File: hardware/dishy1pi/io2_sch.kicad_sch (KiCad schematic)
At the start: 31 parts, among them CN6 KF2EDGR-2.54-9P, CN7 KF2EDGR-2.54-6P, U10 LTV-827S-TA1, U11 LTV-817S-TA1, U12 LTV-817S-TA1, U9 LTV-847S

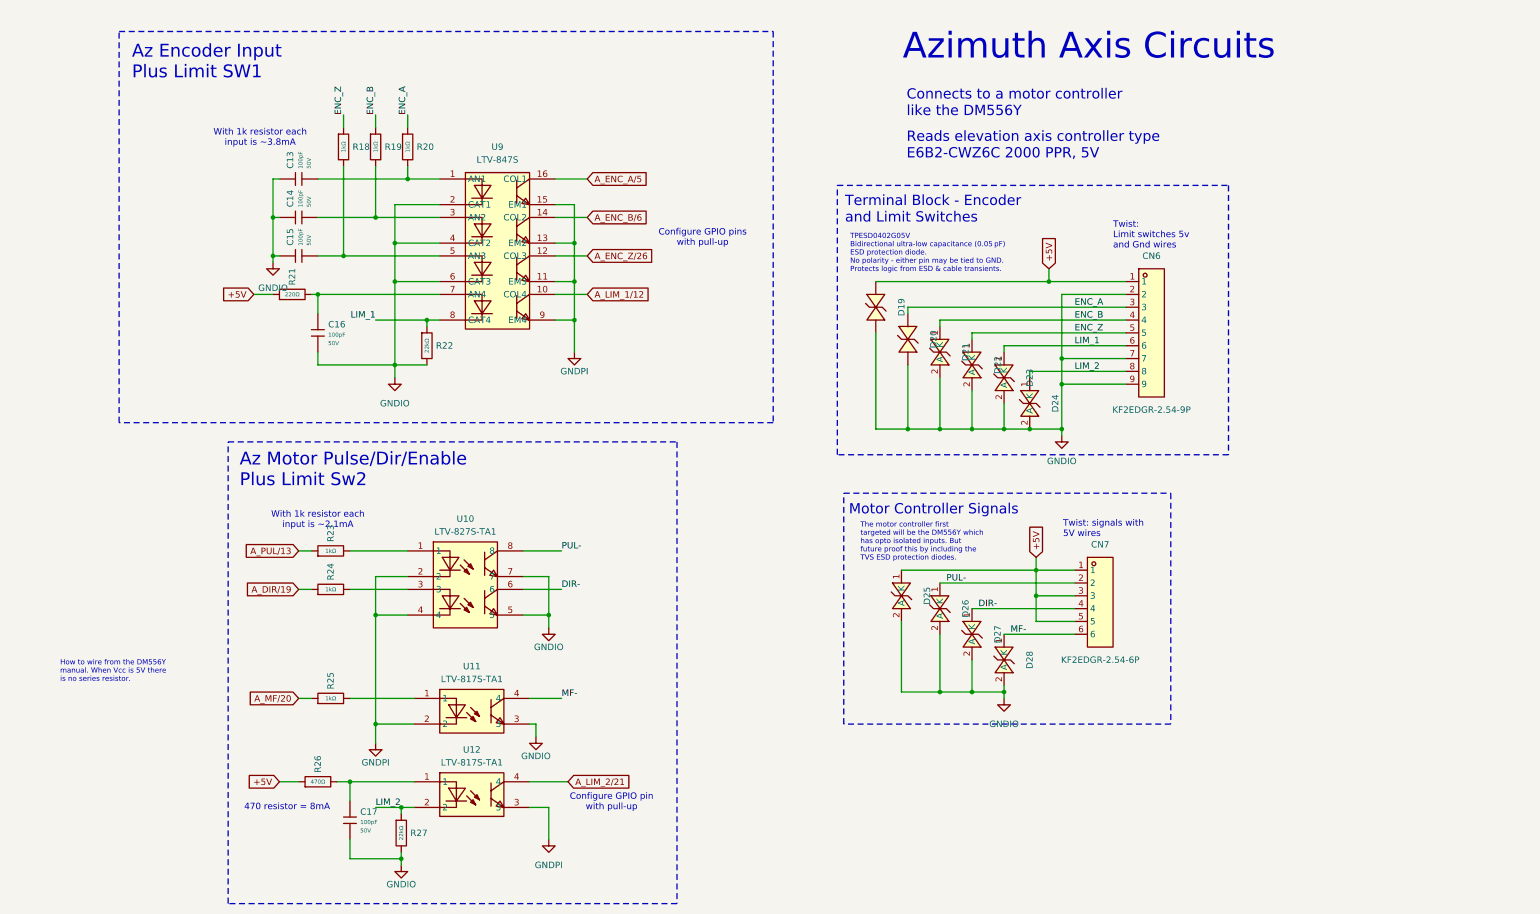
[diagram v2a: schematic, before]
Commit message: Modifications based on first board assembly
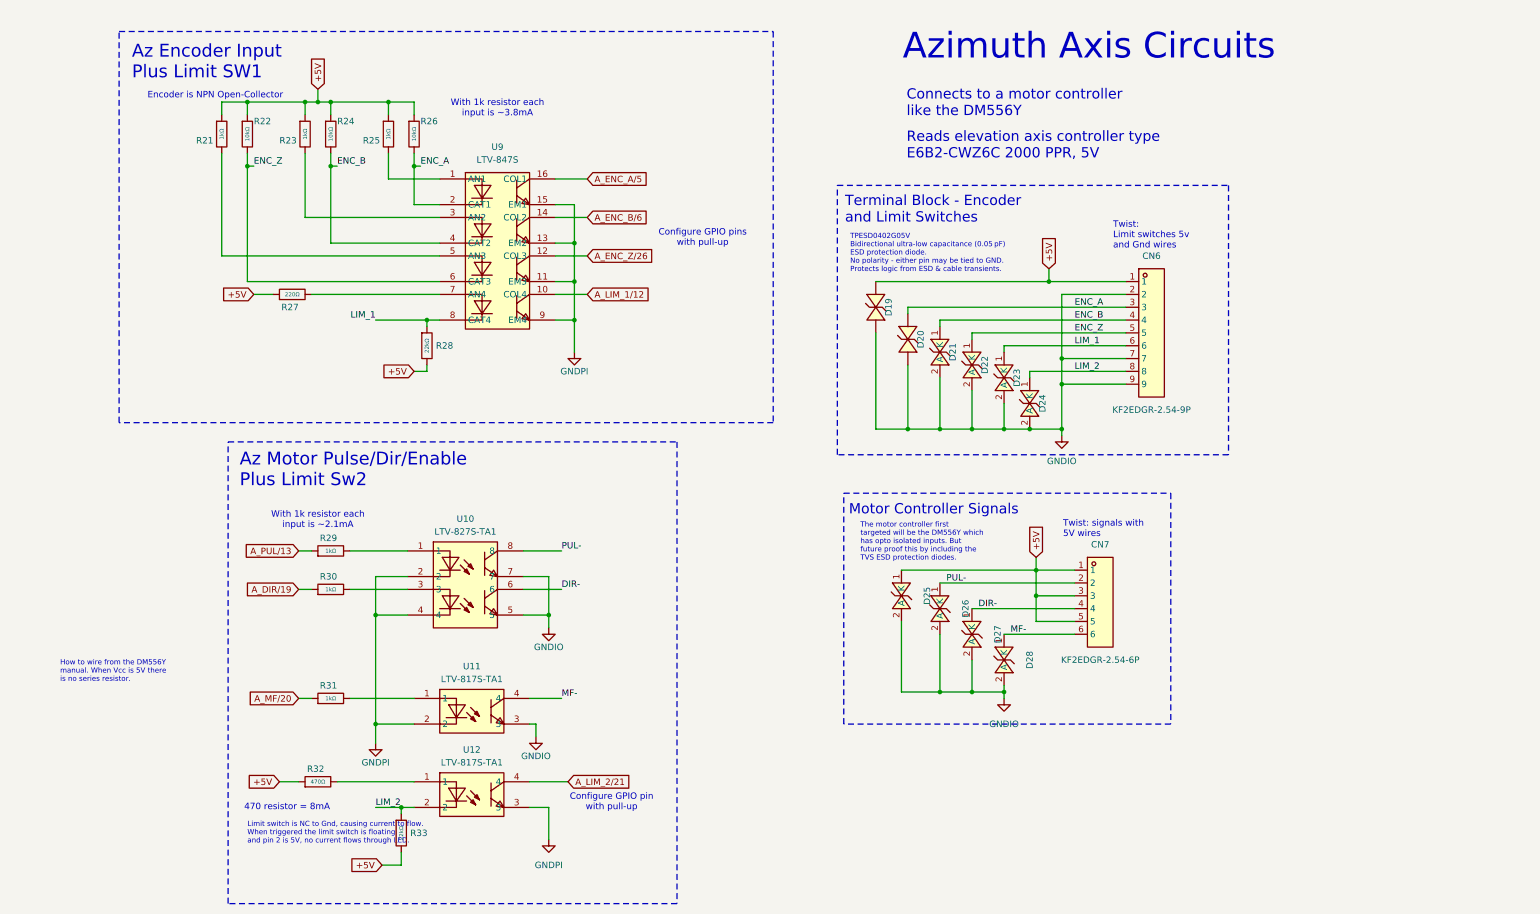
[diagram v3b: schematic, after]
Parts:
- removed C13, C14, C15, C16, C17: 100pF, PCM_JLCPCB:C_0402, symbol PCM_JLCPCB-Capacitors:0402,100pF
- removed R18, R19, R20: 1kΩ, PCM_JLCPCB:R_0402, symbol PCM_JLCPCB-Resistors:0402,1kΩ
- added R21, R23, R25: 1kΩ, PCM_JLCPCB:R_0402, symbol PCM_JLCPCB-Resistors:0402,1kΩ
- added R22, R24, R26: 10kΩ, PCM_JLCPCB:R_0402, symbol PCM_JLCPCB-Resistors:0402,10kΩ
- renumbered R21 to R27, R22 to R28, R23 to R29, R24 to R30, R25 to R31, R26 to R32, R27 to R33
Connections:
- net +5V: now also R28.2, R33.2, R21.1, R22.1, R23.1, R24.1, R25.1, R26.1
- net ENC_A: now also U9.2 (CAT1), R26.2
- net ENC_B: now also U9.4 (CAT2), R24.2
- net ENC_Z: now also U9.6 (CAT3), R22.2
- net GNDIO: no longer R28.2, R33.2, U9.2 (CAT1), U9.4 (CAT2), U9.6 (CAT3)
- net at U9.1 (AN1): now also R25.2
- net at U9.3 (AN2): now also R23.2
- net at U9.5 (AN3): now also R21.2
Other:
- note added: "Encoder is NPN Open-Collector"
- note added: "Limit switch is NC to Gnd, causing current to flow. When triggered the limit switch is floating and pin 2 is 5V, no current flows through LED."

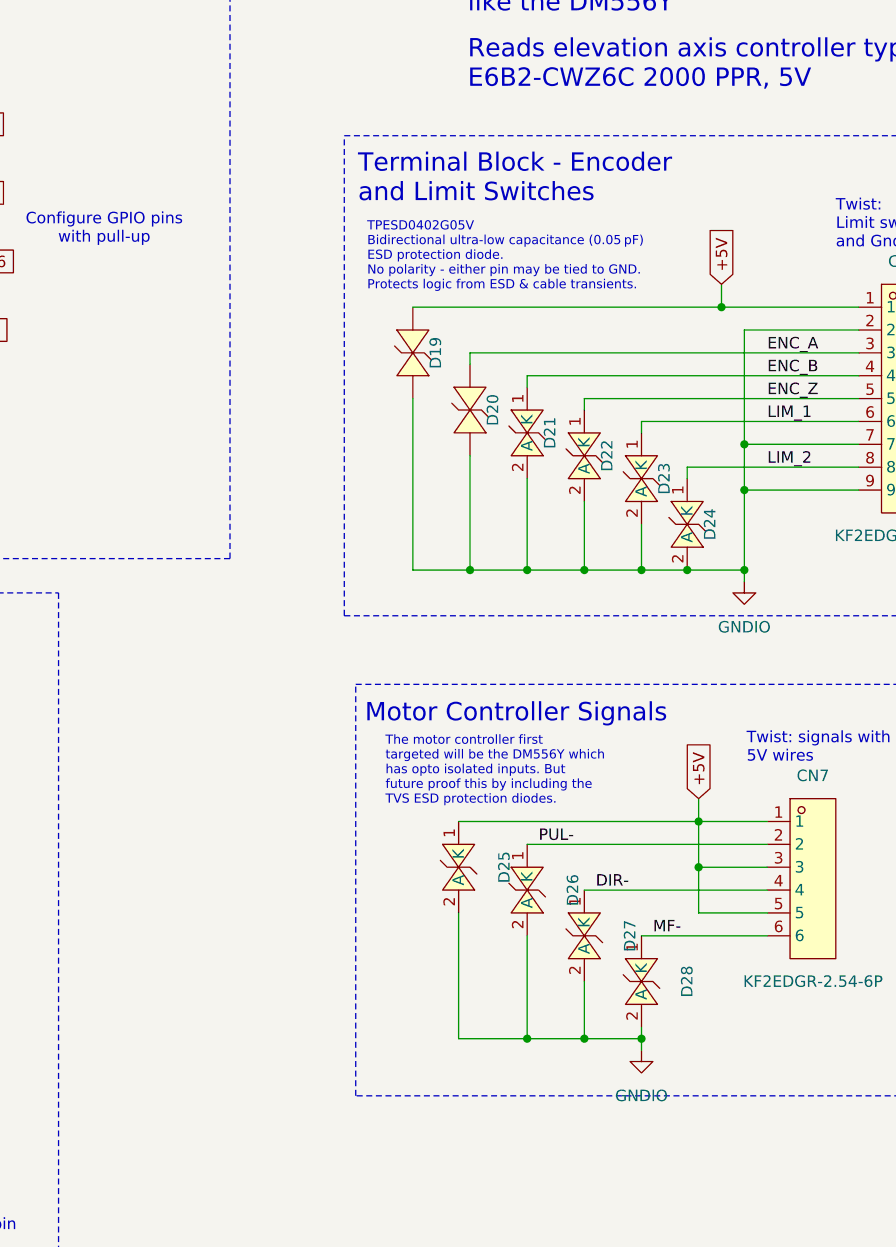
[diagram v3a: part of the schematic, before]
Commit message: Added power circuit to dishy schematic
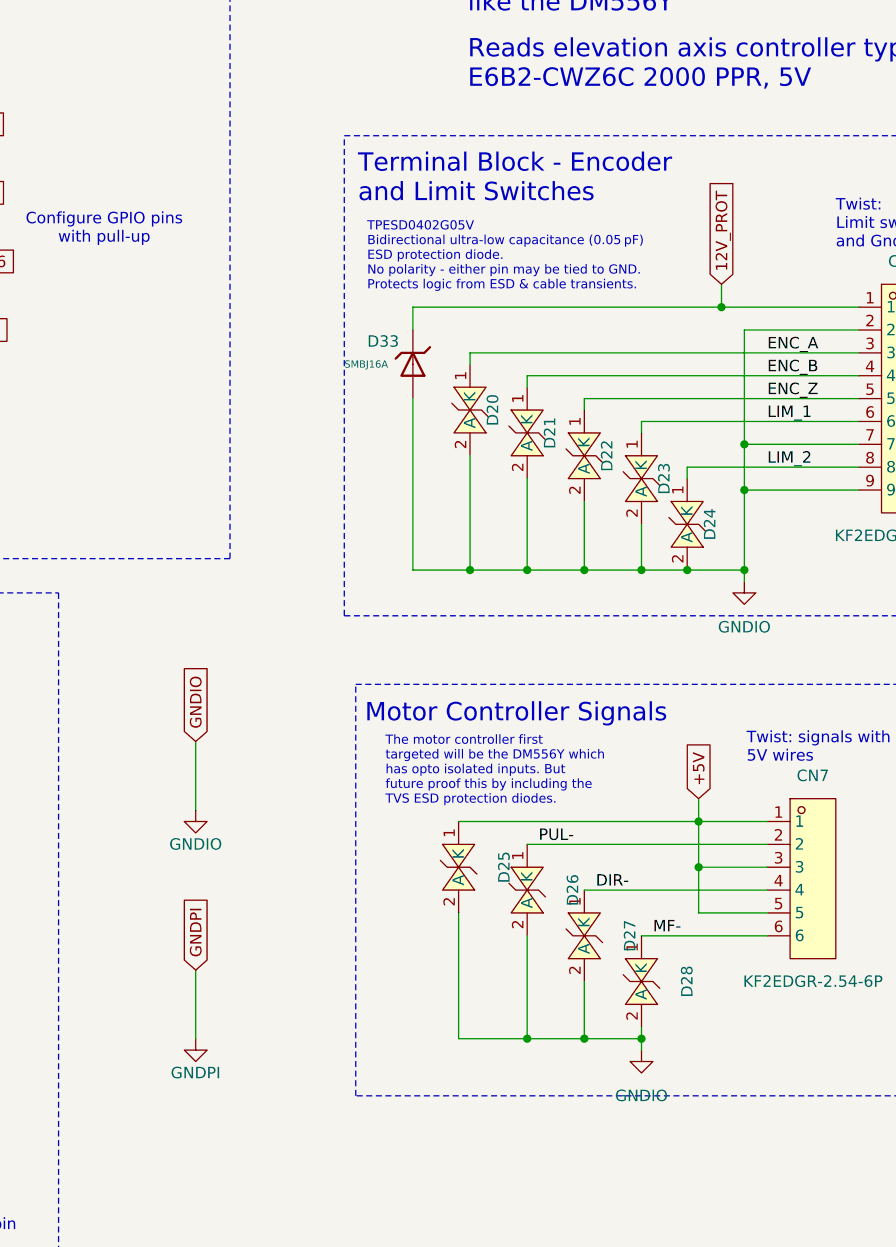
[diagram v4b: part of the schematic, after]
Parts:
- removed D19: TPESD0402G05V, MyParts:D0402-BI, symbol MyParts:TPESD0402G05V
- added D33: SMBJ16A, PCM_JLCPCB:D_SMB, symbol PCM_JLCPCB-Diodes:TVS-Uni,SMBJ16A
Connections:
- net +5V: no longer CN6.1
- net GNDIO: now also D33.2
- new net 12V_PROT: CN6.1, D33.1

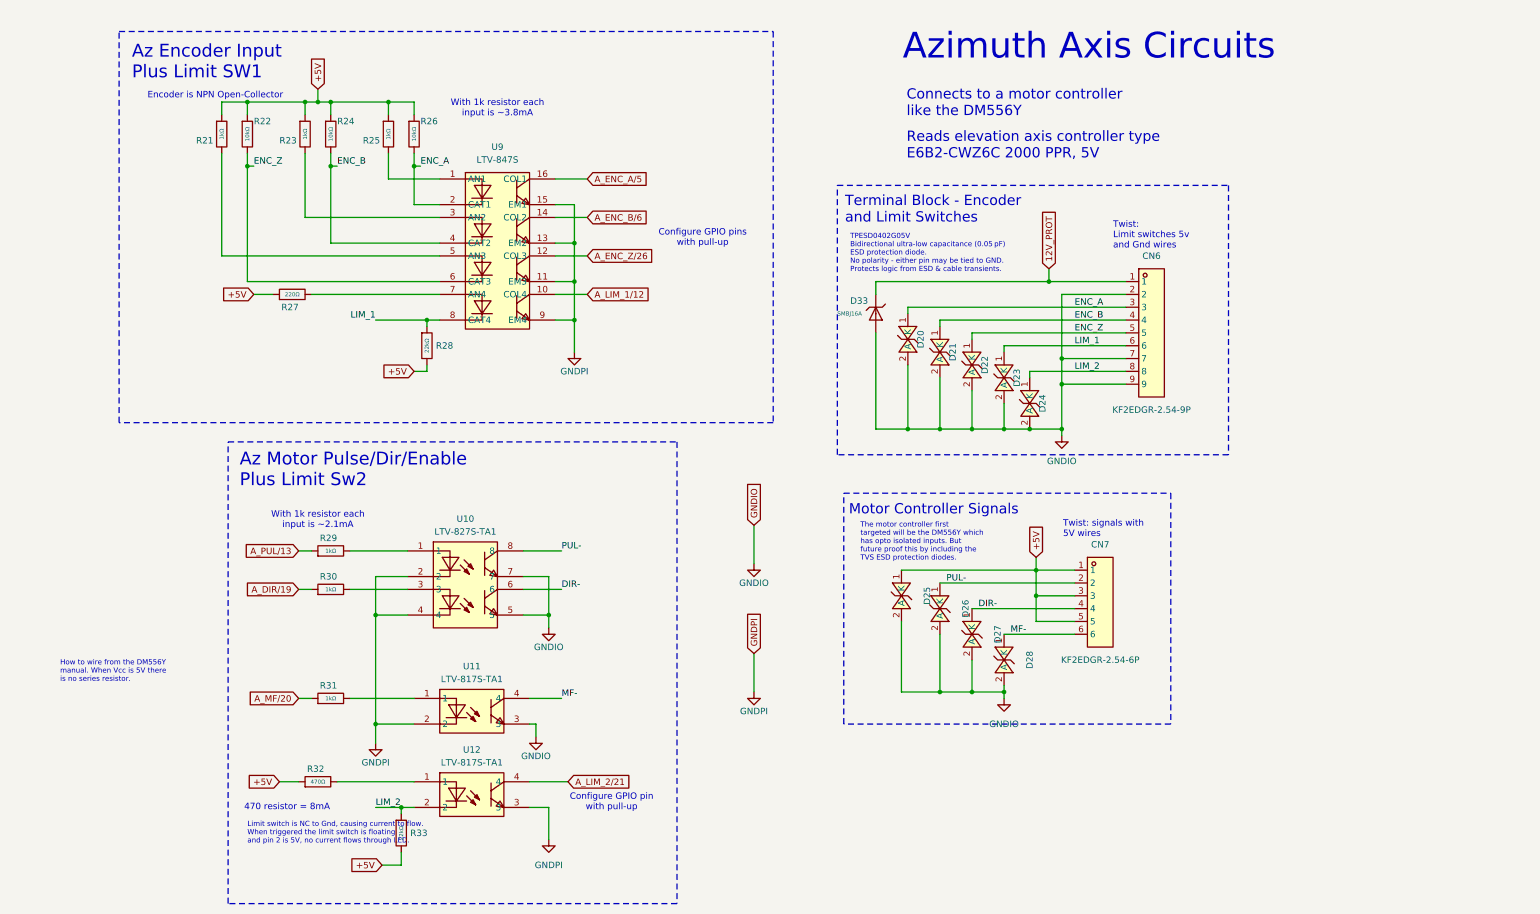
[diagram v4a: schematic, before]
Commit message: Added 12V power input
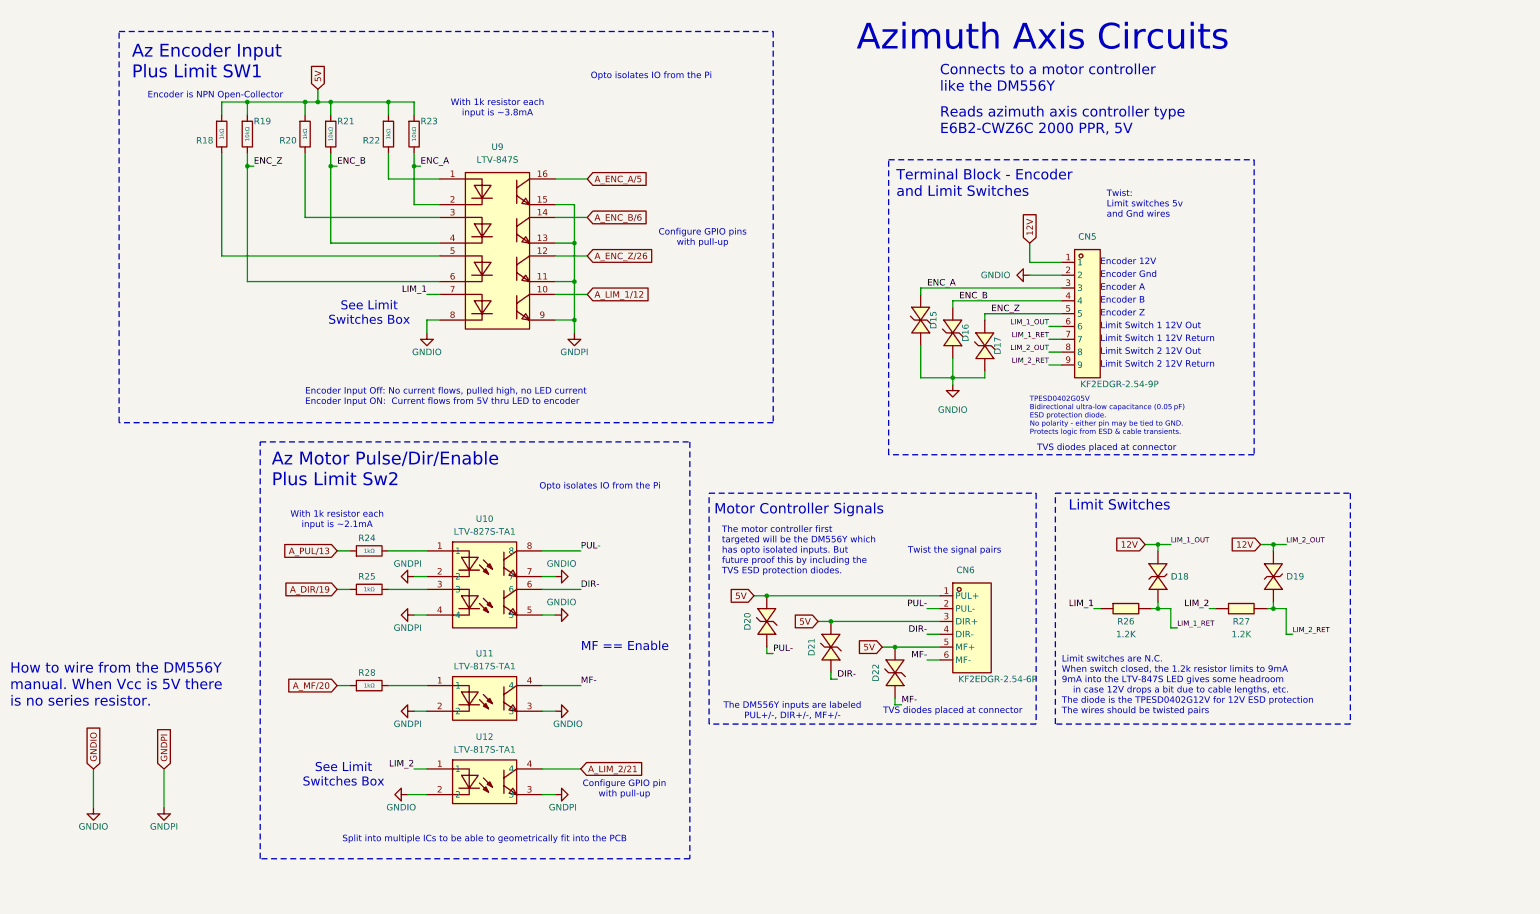
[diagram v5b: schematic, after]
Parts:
- removed D23, D24, D26, D27, D28: TPESD0402G05V, MyParts:D0402-BI, symbol MyParts:TPESD0402G05V
- removed D33: SMBJ16A, PCM_JLCPCB:D_SMB, symbol PCM_JLCPCB-Diodes:TVS-Uni,SMBJ16A
- removed R27: 220Ω, PCM_JLCPCB:R_0402, symbol PCM_JLCPCB-Resistors:0402,220Ω
- removed R28, R33: 22kΩ, PCM_JLCPCB:R_0402, symbol PCM_JLCPCB-Resistors:0402,22kΩ
- removed R32: 470Ω, PCM_JLCPCB:R_0402, symbol PCM_JLCPCB-Resistors:0402,470Ω
- added D18, D19: TPESD0402G12V, MyParts:D0402-BI, symbol MyParts:TPESD0402G12V
- added D21, D22: TPESD0402G05V, MyParts:D0402-BI, symbol MyParts:TPESD0402G05V
- added R26, R27: 1.2K, MyParts:R1206, symbol MyParts:1206W4F1201T5E
- renumbered CN6 to CN5, CN7 to CN6, D20 to D15, D21 to D16, D22 to D17, D25 to D20, R21 to R18, R22 to R19, R23 to R20, R24 to R21, R25 to R22, R26 to R23, R29 to R24, R30 to R25, R31 to R28
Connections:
- net DIR-: now also D21.2 (A)
- net GNDIO: now also U12.2, U9.8 (CAT4); no longer CN5.7, CN5.9, D20.2 (A)
- net LIM_1: now also U9.7 (AN4), R26.1; no longer CN5.6, U9.8 (CAT4)
- net LIM_2: now also U12.1, R27.1; no longer CN5.8, U12.2
- net MF-: now also D22.2 (A)
- net PUL-: now also D20.2 (A)
- net +5V renamed 5V
- net 5V: now also D21.1 (K), D22.1 (K)
- net 12V_PROT renamed 12V
- net 12V: now also CN5.6, CN5.8, D18.1, D19.1
- new net LIM_1_RET: CN5.7, D18.2, R26.2
- new net LIM_2_RET: CN5.9, D19.2, R27.2
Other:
- note added: "Encoder 12V"
- note added: "Encoder A"
- note added: "Encoder B"
- note added: "Encoder Gnd"
- note added: "Encoder Input Off: No current flows, pulled high, no LED current Encoder Input ON: Current flows from 5V thru LED to encoder"
- note added: "Encoder Z"
- note added: "Limit Switch 1 12V Out"
- note added: "Limit Switch 1 12V Return"
- note added: "Limit Switch 2 12V Out"
- note added: "Limit Switch 2 12V Return"
- note added: "Limit Switches"
- note added: "Limit switches are N.C. When switch closed, the 1.2k resistor limits to 9mA 9mA into the LTV-847S LED gives some headroom in case 12V drops a bit due to cable lengths, etc. The diode is the TPESD0402G12V for 12V ESD protection The wires should be twisted pairs"
- note added: "MF == Enable"
- note added: "Opto isolates IO from the Pi"
- note added: "Reads azimuth axis controller type E6B2-CWZ6C 2000 PPR, 5V"
- note added: "See Limit Switches Box"
- note added: "Split into multiple ICs to be able to geometrically fit into the PCB"
- note added: "TVS diodes placed at connector"
- note added: "The DM556Y inputs are labeled PUL+/-, DIR+/-, MF+/-"
- note added: "Twist the signal pairs"
- note removed: "470 resistor = 8mA"
- note removed: "Limit switch is NC to Gnd, causing current to flow. When triggered the limit switch is floating and pin 2 is 5V, no current flows through LED."
- note removed: "Reads elevation axis controller type E6B2-CWZ6C 2000 PPR, 5V"
- note removed: "Twist: signals with 5V wires"
- moved on the sheet: CN5, CN6, R24, R25, R28, U10, U11, U12
